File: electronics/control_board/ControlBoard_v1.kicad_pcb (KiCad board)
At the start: 2 copper layers, 64 x 85 mm, 28 parts, among them J1 Motor1, J2 Motor2, J3 Motor3, J4 Encoder, J5 I2C, J7 Power, U1 ROB-14450, U2 ROB-14450, U3 ROB-14450, U4 DCDC_Converter

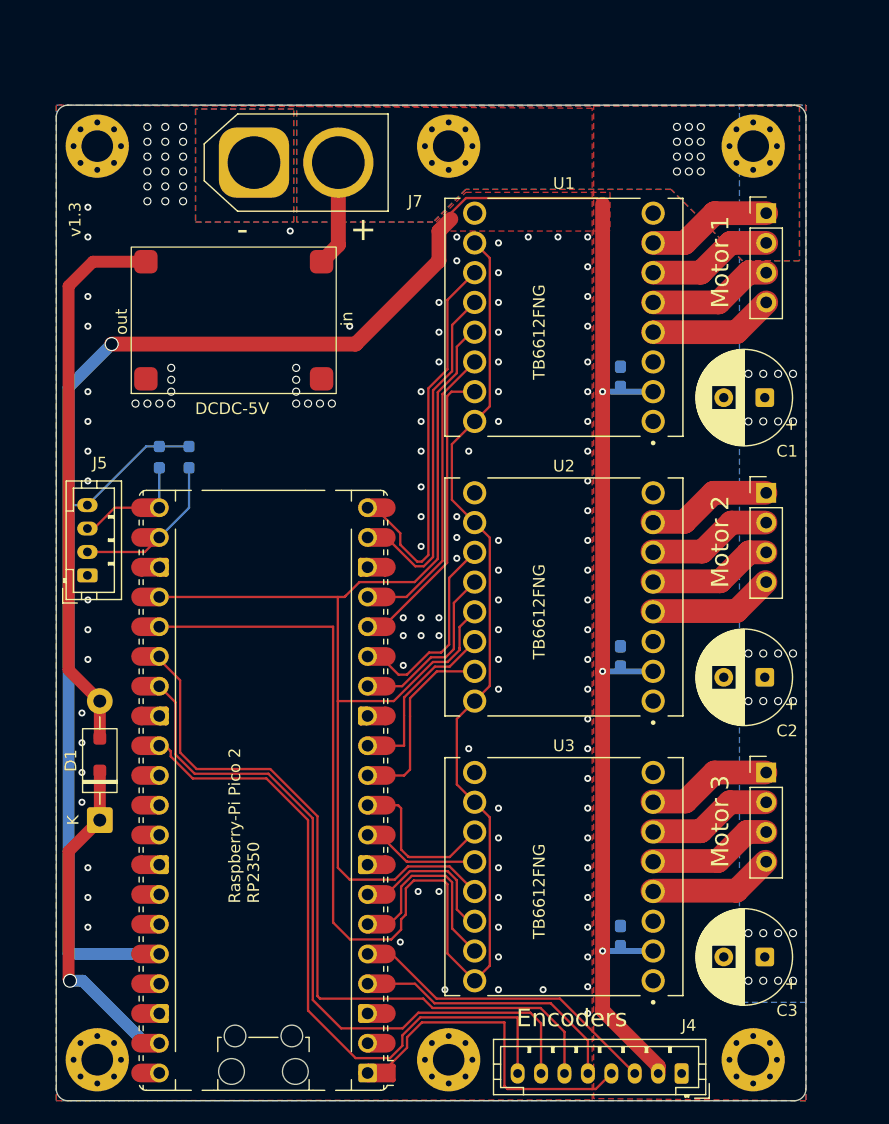
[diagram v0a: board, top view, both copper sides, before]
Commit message: Worked on PCB (moved to 4 layers)
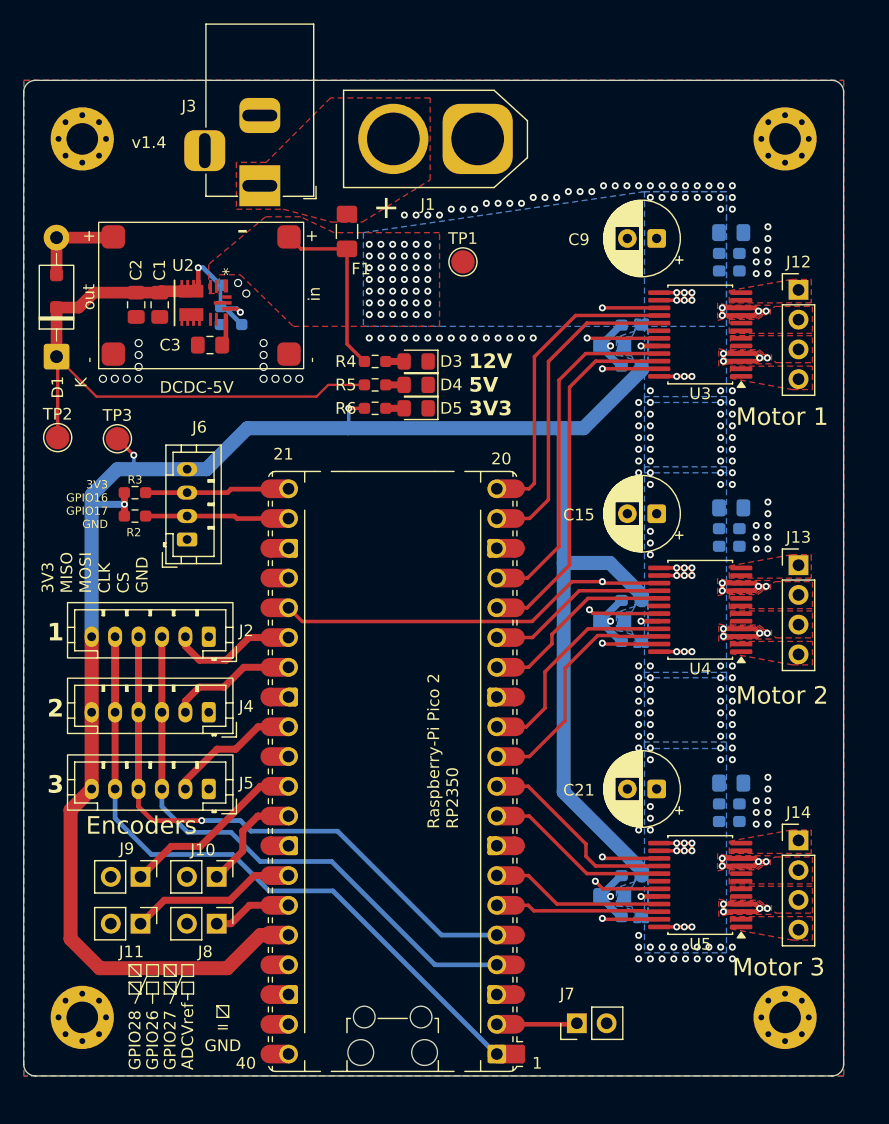
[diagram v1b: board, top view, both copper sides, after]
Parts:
- removed the H5 at (188.3, 120.6)
- removed H6: MountingHole_Pad, MountingHole:MountingHole_2.7mm_M2.5_Pad_Via
- removed the J1 at (215.4, 48.3)
- removed the U1 at (198.1, 57.2)
- added C10: 10u, Capacitor_SMD:C_0805_2012Metric_Pad1.18x1.45mm_HandSolder, B.Cu at (202.2, 83.2)
- added C11: 0.1u, Capacitor_SMD:C_0603_1608Metric_Pad1.08x0.95mm_HandSolder, B.Cu at (203.9, 84.9)
- added C12: 0.1u, Capacitor_SMD:C_0603_1608Metric_Pad1.08x0.95mm_HandSolder, B.Cu at (212.2, 75.3)
- added C13: 0.1u, Capacitor_SMD:C_0603_1608Metric_Pad1.08x0.95mm_HandSolder, B.Cu at (212.2, 76.8)
- added C14: 10u, Capacitor_SMD:C_0805_2012Metric_Pad1.18x1.45mm_HandSolder, B.Cu at (212.4, 73.5)
- added C15: 50u, Capacitor_THT:CP_Radial_D6.3mm_P2.50mm, F.Cu at (206.0, 74.0)
- added C16: 10u, Capacitor_SMD:C_0805_2012Metric_Pad1.18x1.45mm_HandSolder, B.Cu at (202.2, 106.7)
- added C17: 0.1u, Capacitor_SMD:C_0603_1608Metric_Pad1.08x0.95mm_HandSolder, B.Cu at (203.9, 108.4)
- added C18: 0.1u, Capacitor_SMD:C_0603_1608Metric_Pad1.08x0.95mm_HandSolder, B.Cu at (212.2, 98.8)
- added C19: 0.1u, Capacitor_SMD:C_0603_1608Metric_Pad1.08x0.95mm_HandSolder, B.Cu at (212.2, 100.3)
- added C20: 10u, Capacitor_SMD:C_0805_2012Metric_Pad1.18x1.45mm_HandSolder, B.Cu at (212.4, 97.0)
- added C21: 50u, Capacitor_THT:CP_Radial_D6.3mm_P2.50mm, F.Cu at (206.0, 97.5)
- added C22: 0.1u, Capacitor_SMD:C_0603_1608Metric_Pad1.08x0.95mm_HandSolder, B.Cu at (203.9, 57.9)
- added C23: 0.1u, Capacitor_SMD:C_0603_1608Metric_Pad1.08x0.95mm_HandSolder, B.Cu at (203.9, 81.4)
- added C24: 0.1u, Capacitor_SMD:C_0603_1608Metric_Pad1.08x0.95mm_HandSolder, B.Cu at (203.9, 104.9)
- added C7: 0.1u, Capacitor_SMD:C_0603_1608Metric_Pad1.08x0.95mm_HandSolder, B.Cu at (212.2, 53.3)
- added C8: 10u, Capacitor_SMD:C_0805_2012Metric_Pad1.18x1.45mm_HandSolder, B.Cu at (212.4, 50.0)
- added C9: 50u, Capacitor_THT:CP_Radial_D6.3mm_P2.50mm, F.Cu at (206.0, 50.5)
- added D3: 12V_OK, LED_SMD:LED_0805_2012Metric_Pad1.15x1.40mm_HandSolder, F.Cu at (185.5, 61.0)
- added D4: 5V_OK, LED_SMD:LED_0805_2012Metric_Pad1.15x1.40mm_HandSolder, F.Cu at (185.5, 63.0)
- added D5: 3V3_OK, LED_SMD:LED_0805_2012Metric_Pad1.15x1.40mm_HandSolder, F.Cu at (185.5, 65.0)
- added F1: Fuse, Fuse:Fuse_1206_3216Metric_Pad1.42x1.75mm_HandSolder, F.Cu at (179.6, 49.9)
- added J10: Conn_01x02_Pin, Connector_PinHeader_2.54mm:PinHeader_1x02_P2.54mm_Vertical, F.Cu at (168.5, 105.0)
- added J11: Conn_01x02_Pin, Connector_PinHeader_2.54mm:PinHeader_1x02_P2.54mm_Vertical, F.Cu at (162.0, 109.0)
- added J12: Motor1, Connector_PinHeader_2.54mm:PinHeader_1x04_P2.54mm_Vertical, F.Cu at (218.1, 54.9)
- added J13: Motor1, Connector_PinHeader_2.54mm:PinHeader_1x04_P2.54mm_Vertical, F.Cu at (218.1, 78.4)
- added J14: Motor1, Connector_PinHeader_2.54mm:PinHeader_1x04_P2.54mm_Vertical, F.Cu at (218.1, 101.9)
- added J5: Conn_01x06_Pin, Connector_JST:JST_PH_B6B-PH-K_1x06_P2.00mm_Vertical, F.Cu at (167.8, 97.5)
- added J7: Conn_01x02_Pin, Connector_PinHeader_2.54mm:PinHeader_1x02_P2.54mm_Vertical, F.Cu at (199.2, 117.5)
- added J8: Conn_01x02_Pin, Connector_PinHeader_2.54mm:PinHeader_1x02_P2.54mm_Vertical, F.Cu at (168.5, 109.0)
- added J9: Conn_01x02_Pin, Connector_PinHeader_2.54mm:PinHeader_1x02_P2.54mm_Vertical, F.Cu at (162.0, 105.0)
- added R1: TBD, Resistor_SMD:R_0603_1608Metric_Pad0.98x0.95mm_HandSolder, B.Cu at (169.7, 57.8)
- added R4: 1k, Resistor_SMD:R_0603_1608Metric_Pad0.98x0.95mm_HandSolder, F.Cu at (182.0, 61.0)
- added R5: 1k, Resistor_SMD:R_0603_1608Metric_Pad0.98x0.95mm_HandSolder, F.Cu at (182.0, 63.0)
- added R6: 1k, Resistor_SMD:R_0603_1608Metric_Pad0.98x0.95mm_HandSolder, F.Cu at (182.0, 65.0)
- added RJ1: TBD, Additions:0603_shorted_resistor, B.Cu at (168.8, 55.4)
- added TP1: 12V, TestPoint:TestPoint_Pad_D2.0mm, F.Cu at (189.5, 52.5)
- added TP2: 5V, TestPoint:TestPoint_Pad_D2.0mm, F.Cu at (154.9, 67.5)
- added TP3: 3V3, TestPoint:TestPoint_Pad_D2.0mm, F.Cu at (160.0, 67.6)
- added U4: TB6612FNG, Package_SO:SSOP-24_5.3x8.2mm_P0.65mm, F.Cu at (209.8, 82.2)
- added U5: TB6612FNG, Package_SO:SSOP-24_5.3x8.2mm_P0.65mm, F.Cu at (209.8, 105.7)
- C1, C2: value C_Polarized -> 22u; footprint Capacitor_THT:CP_Radial_D8.0mm_P3.50mm -> Capacitor_SMD:C_0805_2012Metric_Pad1.18x1.45mm_HandSolder
- C3: value C_Polarized -> 1u; footprint Capacitor_THT:CP_Radial_D8.0mm_P3.50mm -> Capacitor_SMD:C_0805_2012Metric_Pad1.18x1.45mm_HandSolder
- C4: value C -> 10u; footprint Capacitor_SMD:C_0603_1608Metric_Pad1.08x0.95mm_HandSolder -> Capacitor_SMD:C_0805_2012Metric_Pad1.18x1.45mm_HandSolder
- C5, C6: value C -> 0.1u
- J2: value Motor2 -> Conn_01x06_Pin; footprint Connector_PinHeader_2.54mm:PinHeader_1x04_P2.54mm_Vertical -> Connector_JST:JST_PH_B6B-PH-K_1x06_P2.00mm_Vertical
- J3: value Motor3 -> Barrel_Jack_Switch; footprint Connector_PinHeader_2.54mm:PinHeader_1x04_P2.54mm_Vertical -> Connector_BarrelJack:BarrelJack_Horizontal
- J4: value Encoder -> Conn_01x06_Pin; footprint Connector_JST:JST_PH_B8B-PH-K_1x08_P2.00mm_Vertical -> Connector_JST:JST_PH_B6B-PH-K_1x06_P2.00mm_Vertical
- R2: moved to F.Cu
- R3: renamed from R1; moved to F.Cu
- U2: value ROB-14450 -> TPSM33610S5QRDNRQ1; footprint ROB-14450:MODULE_ROB-14450 -> Additions:TPSM33610S5QRDNRQ1
- U3: value ROB-14450 -> TB6612FNG; footprint ROB-14450:MODULE_ROB-14450 -> Package_SO:SSOP-24_5.3x8.2mm_P0.65mm
- moved C3 70.5 mm to (167.9, 59.6)
- moved J3 66.2 mm to (172.2, 46.0), turned to -90 degrees
- moved C2 62.4 mm to (161.6, 56.2), turned to -90 degrees
- moved C6 59.0 mm to (212.2, 51.8), turned to 0 degrees
- moved C1 52.3 mm to (163.6, 56.2), turned to -90 degrees
- moved J4 50.8 mm to (167.8, 91.0)
- moved J2 49.2 mm to (167.8, 84.5), turned to 180 degrees
- moved U3 47.7 mm to (209.8, 58.7)
- moved U2 39.8 mm to (167.3, 56.0), turned to -90 degrees
- moved D1 39.7 mm to (154.8, 60.6)
- moved D2 39.7 mm to (154.8, 55.0)
- moved C5 24.8 mm to (203.9, 61.4), turned to 180 degrees
- moved J1 19.2 mm to (190.8, 42.0), turned to 180 degrees
- moved REF** 17.3 mm to (166.2, 116.2)
- moved A1 11.2 mm to (183.5, 96.0)
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- renumbered H4 to H2, H2 to H3, H3 to H5, J7 to J1, J5 to J6, U4 to U1
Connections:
- A1 pad 2: unconnected-(A1-GPIO1-Pad2)_1 -> /GPIO1
- A1 pad 31: unconnected-(A1-GPIO26_ADC0-Pad31)_1 -> /GPIO26_ADC0
- A1 pad 32: unconnected-(A1-GPIO27_ADC1-Pad32)_1 -> /GPIO27_ADC1
- A1 pad 34: unconnected-(A1-GPIO28_ADC2-Pad34)_1 -> /GPIO28_ADC2
- A1 pad 35: unconnected-(A1-ADC_VREF-Pad35)_1 -> /ADC_VREF
- C1 pad 1: +12V -> +5V
- C2 pad 1: +12V -> +5V
- C3 pad 1: +12V -> Net-(U2-VCC)
- C6 pad 1: +3.3V -> +12V
- H1 pad 1: unconnected-(H1-Pad1)_6 -> GND
- H2 pad 1: unconnected-(H4-Pad1)_5 -> GND
- H3 pad 1: unconnected-(H2-Pad1)_2 -> GND
- H5 pad 1: unconnected-(H3-Pad1)_6 -> GND
- J1 pad 2: +12V -> Net-(J1-Pin_2)
- J2 pad 1: Net-(J2-Pin_1) -> GND
- J2 pad 2: Net-(J2-Pin_2) -> /Encoder1_CS
- J2 pad 3: Net-(J2-Pin_3) -> /Encoder_SCK
- J2 pad 4: Net-(J2-Pin_4) -> /Encoder_MOSI
- J3 pad 1: Net-(J3-Pin_1) -> Net-(J1-Pin_2)
- J3 pad 2: Net-(J3-Pin_2) -> GND
- J3 pad 3: Net-(J3-Pin_3) -> GND
- J4 pad 2: +3.3V -> /Encoder2_CS
- J4 pad 3: /Encoder_MOSI -> /Encoder_SCK
- J4 pad 4: /Encoder_MISO -> /Encoder_MOSI
- J4 pad 5: /Encoder_SCK -> /Encoder_MISO
- J4 pad 6: /Encoder1_CS -> +3.3V
- U2 pad 1: +12V -> unconnected-(U2-PGOOD-Pad1)
- U2 pad 10: /MotorPWM -> GND
- U2 pad 11: /Motor2_B2 -> GND
- U2 pad 2: +3.3V -> +12V
- U2 pad 3: GND -> +12V
- U2 pad 4: Net-(J2-Pin_4) -> +5V
- U2 pad 5: Net-(J2-Pin_3) -> unconnected-(U2-SW-Pad5)
- U2 pad 6: Net-(J2-Pin_2) -> unconnected-(U2-SW-Pad6)
- U2 pad 7: Net-(J2-Pin_1) -> unconnected-(U2-BOOT-Pad7)
- U2 pad 8: GND -> Net-(U2-VCC)
- U2 pad 9: GND -> Net-(U2-FB)
- U3 pad 1: +12V -> Net-(J12-Pin_4)
- U3 pad 10: /MotorPWM -> GND
- U3 pad 11: /Motor3_B2 -> Net-(J12-Pin_1)
- U3 pad 12: /Motor3_B1 -> Net-(J12-Pin_1)
- U3 pad 13: /MotorEN -> +12V
- U3 pad 14: /Motor3_A1 -> +12V
- U3 pad 15: /Motor3_A2 -> /MotorPWM
- U3 pad 16: /MotorPWM -> /Motor1_B2
- U3 pad 2: +3.3V -> Net-(J12-Pin_4)
- U3 pad 4: Net-(J3-Pin_4) -> GND
- U3 pad 5: Net-(J3-Pin_3) -> Net-(J12-Pin_3)
- U3 pad 6: Net-(J3-Pin_2) -> Net-(J12-Pin_3)
- U3 pad 7: Net-(J3-Pin_1) -> Net-(J12-Pin_2)
- U3 pad 8: GND -> Net-(J12-Pin_2)
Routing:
- net +5V: track 28.4 -> 127.8 mm
- net GND: track 0.00 -> 64.6 mm, vias 129 -> 163
- net /Encoder1_CS: track 64.2 -> 10.1 mm
- net /Encoder2_CS: track 61.6 -> 10.2 mm
- net /Encoder3_CS: track 58.2 -> 10.6 mm
- net Net-(D1-A): track 47.2 -> 7.96 mm
- net +12V: track 9.05 -> 47.0 mm, vias 36 -> 126
- net +3.3V: track 211.7 -> 176.5 mm, vias 4 -> 6
- net /Encoder_MISO: track 29.4 -> 62.8 mm
- net /Encoder_SCK: track 23.8 -> 48.7 mm
- net /MotorPWM: track 132.8 -> 111.4 mm, vias 0 -> 6
- net /Encoder_MOSI: track 28.8 -> 49.6 mm, vias 0 -> 1
- net /GPIO26_ADC0: track 0.00 -> 15.0 mm
- net /GPIO28_ADC2: track 0.00 -> 13.5 mm
- net Net-(J1-Pin_4): track 10.7 -> 0.00 mm
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- added copper zone on In2.Cu, net +12V
- added copper zone on B.Cu, net +3.3V
- added copper zone on In1.Cu, net GND
- added copper zone on F.Cu, net Net-(J1-Pin_2)
- added copper zone on F.Cu, net Net-(J12-Pin_1)
- added copper zone on F.Cu, net Net-(J12-Pin_2)
- added copper zone on F.Cu, net Net-(J12-Pin_3)
- added copper zone on F.Cu, net Net-(J12-Pin_4)
- added copper zone on F.Cu, net Net-(J13-Pin_1)
- added copper zone on F.Cu, net Net-(J13-Pin_2)
- added copper zone on F.Cu, net Net-(J13-Pin_3)
- added copper zone on F.Cu, net Net-(J13-Pin_4)
- added copper zone on F.Cu, net Net-(J14-Pin_1)
- added copper zone on F.Cu, net Net-(J14-Pin_2)
- added copper zone on F.Cu, net Net-(J14-Pin_3)
- added copper zone on F.Cu, net Net-(J14-Pin_4)
- removed copper zone on F.Cu, net +3.3V
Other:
- board size 64 x 85 mm -> 70 x 85 mm
- copper layers 2 -> 4
- board text added: "1"
- board text added: "12V 5V 3V3"
- board text added: "2"
- board text added: "20"
- board text added: "21"
- board text added: "3"
- board text added: "3V3 GPIO16 GPIO17 GND"
- board text added: "3V3 MISO MOSI CLK CS GND"
- board text added: "40"
- board text added: "= GND"
- board text added: "ADCVref"
- board text added: "GPIO26"
- board text added: "GPIO27"
- board text added: "GPIO28"
- board text added: "v1.4"
- board text removed: "(00) MISO"
- board text removed: "(03) MOSI"
- board text removed: "(20) CS_1"
- board text removed: "(21) CS_2"
- board text removed: "(22) CS_3"
- board text removed: "(O2) SCK"
- board text removed: "3.3V"
- board text removed: "GND"
- board text removed: "GPIO16"
- board text removed: "GPIO17"
- board text removed: "M1_A1 (13) M1_A2 (12) M1_B1 (14) M1_B2 (15)"
- board text removed: "M2_A1 (09) M2_A2 (08) M2_B1 (10) M2_B2 (11)"
- board text removed: "M3_A1 (05) M3_A2 (04) M3_B1 (06) M3_B2 (07)"
- board text removed: "MotorEN (18)"
- board text removed: "MotorPWM (19)"
- board text removed: "Precision Stepper Controller 3X"
- board text removed: "TB6612FNG"
- board text removed: "v1.3"

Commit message: Worked on schematic and layout Added logo
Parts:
- added C1: 0.1u, Capacitor_SMD:C_0603_1608Metric_Pad1.08x0.95mm_HandSolder, F.Cu at (167.6, 51.8)
- added C2: 22u, Capacitor_SMD:C_0805_2012Metric_Pad1.18x1.45mm_HandSolder, F.Cu at (167.4, 50.0)
- added R10: 4K7, Resistor_SMD:R_0603_1608Metric_Pad0.98x0.95mm_HandSolder, B.Cu at (169.7, 79.5)
- added R4: 4K7, Resistor_SMD:R_0603_1608Metric_Pad0.98x0.95mm_HandSolder, B.Cu at (164.9, 94.1)
- added R5: 4K7, Resistor_SMD:R_0603_1608Metric_Pad0.98x0.95mm_HandSolder, B.Cu at (164.9, 87.9)
- added R6: 4K7, Resistor_SMD:R_0603_1608Metric_Pad0.98x0.95mm_HandSolder, B.Cu at (164.9, 81.8)
- added REF**: Logo, Additions:Logo, F.Cu at (183.4, 88.0)
- C12: renamed from C9; value 50u -> 100u
- C19: renamed from C15; value 50u -> 100u
- C26: renamed from C21; value 50u -> 100u
- F1: value Fuse -> 7A
- J12, J13, J14: value Motor1 -> ~
- R7: renamed from R4; value 1k -> 4k7
- moved R2 2.00 mm to (161.5, 72.2)
- moved R3 2.00 mm to (161.5, 74.2)
- moved D5 0.10 mm to (185.5, 64.9)
- moved R9 0.10 mm to (182.0, 64.9)
- renumbered C7 to C10, C8 to C11, C10 to C13, C11 to C14, C23 to C15, C12 to C16, C13 to C17, C14 to C18, C16 to C20, C17 to C21, C24 to C22, C18 to C23, C19 to C24, C20 to C25, C1 to C3, C2 to C4, C3 to C5, C4 to C6, C5 to C7, C22 to C8, C6 to C9, H5 to H4, R5 to R8, R6 to R9
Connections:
- A1 pad 21: /I2C_SCL -> /I2C_SDA
- A1 pad 22: /I2C_SDA -> /I2C_SCL
- R2 pad 2: /I2C_SDA -> /I2C_SCL
- R3 pad 2: /I2C_SCL -> /I2C_SDA
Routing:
- net +3.3V: track 176.5 -> 199.1 mm
- net +12V: track 47.0 -> 66.6 mm
- net /I2C_SCL: track 11.5 -> 19.0 mm
- net /MotorEN: track 90.7 -> 94.7 mm
- net /Encoder3_CS: track 10.6 -> 14.0 mm
- net /Encoder2_CS: track 10.2 -> 13.2 mm
- net /Encoder1_CS: track 10.1 -> 12.7 mm
- net /I2C_SDA: track 11.5 -> 12.4 mm

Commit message: Worked on PCB and Schematic, created production files
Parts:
- added D3: SMAJ12CA, Diode_SMD:D_SMA_Handsoldering, B.Cu at (208.8, 45.8)
- moved TP1 1.50 mm to (189.4, 54.0)
- moved C12 1.50 mm to (206.0, 49.0)
- moved REF** 0.39 mm to (183.5, 88.4)
- renumbered D3 to D4, D4 to D5, D5 to D6
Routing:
- net +12V: track 66.6 -> 95.3 mm, vias 126 -> 80
- net +3.3V: track 199.1 -> 227.3 mm, vias 6 -> 27
- net /MotorPWM: track 111.4 -> 121.5 mm
- net +5V: track 127.8 -> 135.0 mm, vias 1 -> 7
- net GND: track 64.6 -> 70.5 mm, vias 163 -> 224
- net /MotorEN: track 94.7 -> 97.8 mm
- net /I2C_SCL: track 19.0 -> 19.9 mm
- added copper zone on F.Cu, net +3.3V
- added copper zone on In2.Cu, net +3.3V
- added copper zone on F.Cu, net +5V
- added copper zone on In2.Cu, net +5V
- added copper zone on In2.Cu, net GND
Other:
- board text added: "12V"
- board text added: "3V3"
- board text added: "5V"
- board text added: "GPIO1 GND"
- board text removed: "= GND"

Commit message: Fixed wrong ordering numbers Regenerated IBOM with corrected settings to exclude TP's
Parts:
- R10, R2, R3, R4, R5, R6: value 4K7 -> 4k7
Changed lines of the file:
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@@
 			)
 		)
+		(property "Distributor" "Digikey"
+			(at 0 0 0)
+			(unlocked yes)
+			(layer "F.Fab")
+			(hide yes)
+			(effects
+				(font
+					(size 1 1)
+					(thickness 0.15)
+				)
+			)
+		)
+		(property "Distributor Number" "541-4.70KHCT-ND"
+			(at 0 0 0)
+			(unlocked yes)
+			(layer "F.Fab")
+			(hide yes)
+			(effects
+				(font
+					(size 1 1)
+					(thickness 0.15)
+				)
+			)
+		)
 		(property ki_fp_filters "R_*")
 		(sheetname "/")
@@
 			)
 		)
+		(property "Distributor" "-"
+			(at 0 0 0)
+			(unlocked yes)
+			(layer "F.Fab")
+			(hide yes)
+			(effects
+				(font
+					(size 1 1)
+					(thickness 0.15)
+				)
+			)
+		)
+		(property "Distributor Number" "-"
+			(at 0 0 0)
+			(unlocked yes)
+			(layer "F.Fab")
+			(hide yes)
+			(effects
+				(font
+					(size 1 1)
+					(thickness 0.15)
+				)
+			)
+		)
 		(property ki_fp_filters "Pin* Test*")
 		(sheetname "/")
@@
 			)
 		)
+		(attr exclude_from_bom)
 		(duplicate_pad_numbers_are_jumpers no)
 		(fp_circle
@@
 			)
 		)
+		(property "Distributor" "?"
+			(at 0 0 180)
+			(unlocked yes)
+			(layer "F.Fab")
+			(hide yes)
+			(effects
+				(font
+					(size 1 1)
+					(thickness 0.15)
+				)
+			)
+		)
+		(property "Distributor Number" "-"
+			(at 0 0 180)
+			(unlocked yes)
+			(layer "F.Fab")
+			(hide yes)
+			(effects
+				(font
+					(size 1 1)
+					(thickness 0.15)
+				)
+			)
+		)
 		(property ki_fp_filters "LED* LED_SMD:* LED_THT:*")
 		(sheetname "/")
@@
 			)
 		)
-		(property "Value" "4K7"
+		(property "Value" "4k7"
 			(at 0 1.43 0)
 			(layer "F.Fab")
@@
 			)
 		)
-		(property "Distributor Number" "455-B6B-XH-A-ND"
+		(property "Distributor Number" "455-1708-ND"
 			(at 0 0 180)
 			(unlocked yes)
@@
 			)
 		)
+		(property "Distributor" "-"
+			(at 0 0 0)
+			(unlocked yes)
+			(layer "F.Fab")
+			(hide yes)
+			(effects
+				(font
+					(size 1 1)
+					(thickness 0.15)
+				)
+			)
+		)
+		(property "Distributor Number" "-"
+			(at 0 0 0)
+			(unlocked yes)
+			(layer "F.Fab")
+			(hide yes)
+			(effects
+				(font
+					(size 1 1)
+					(thickness 0.15)
+				)
+			)
+		)
 		(property ki_fp_filters "Pin* Test*")
 		(sheetname "/")
@@
 			)
 		)
+		(attr exclude_from_bom)
 		(duplicate_pad_numbers_are_jumpers no)
 		(fp_circle
@@
 			)
 		)
+		(property "Distributor" "-"
+			(at 0 0 0)
+			(unlocked yes)
+			(layer "F.Fab")
+			(hide yes)
+			(effects
+				(font
+					(size 1 1)
+					(thickness 0.15)
+				)
+			)
+		)
+		(property "Distributor Number" "-"
+			(at 0 0 0)
+			(unlocked yes)
+			(layer "F.Fab")
+			(hide yes)
+			(effects
+				(font
+					(size 1 1)
+					(thickness 0.15)
+				)
+			)
+		)
 		(property ki_fp_filters "Pin* Test*")
 		(sheetname "/")
@@
 			)
 		)
+		(attr exclude_from_bom)
 		(duplicate_pad_numbers_are_jumpers no)
 		(fp_circle
@@
 			)
 		)
+		(property "Distributor" "?"
+			(at 0 0 180)
+			(unlocked yes)
+			(layer "F.Fab")
+			(hide yes)
+			(effects
+				(font
+					(size 1 1)
+					(thickness 0.15)
+				)
+			)
+		)
+		(property "Distributor Number" "-"
+			(at 0 0 180)
+			(unlocked yes)
+			(layer "F.Fab")
+			(hide yes)
+			(effects
+				(font
+					(size 1 1)
+					(thickness 0.15)
+				)
+			)
+		)
 		(property ki_fp_filters "LED* LED_SMD:* LED_THT:*")
 		(sheetname "/")
@@
 			)
 		)
+		(property "Distributor" "?"
+			(at 0 0 180)
+			(unlocked yes)
+			(layer "F.Fab")
+			(hide yes)
+			(effects
+				(font
+					(size 1 1)
+					(thickness 0.15)
+				)
+			)
+		)
+		(property "Distributor Number" "-"
+			(at 0 0 180)
+			(unlocked yes)
+			(layer "F.Fab")
+			(hide yes)
+			(effects
+				(font
+					(size 1 1)
+					(thickness 0.15)
+				)
+			)
+		)
 		(property ki_fp_filters "LED* LED_SMD:* LED_THT:*")
 		(sheetname "/")
@@
 			)
 		)
+		(property "Distributor" "Digikey"
+			(at 0 0 0)
+			(unlocked yes)
+			(layer "F.Fab")
+			(hide yes)
+			(effects
+				(font
+					(size 1 1)
+					(thickness 0.15)
+				)
+			)
+		)
+		(property "Distributor Number" "541-1.00KHCT-ND"
+			(at 0 0 0)
+			(unlocked yes)
+			(layer "F.Fab")
+			(hide yes)
+			(effects
+				(font
+					(size 1 1)
+					(thickness 0.15)
+				)
+			)
+		)
 		(property ki_fp_filters "R_*")
 		(sheetname "/")
@@
 			)
 		)
-		(property "Distributor Number" "455-B6B-XH-A-ND"
+		(property "Distributor Number" "455-1708-ND"
 			(at 0 0 180)
 			(unlocked yes)
@@
 			)
 		)
-		(property "Distributor Number" "455-B4B-XH-A-ND"
+		(property "Distributor Number" "455-1706-ND"
 			(at 0 0 90)
 			(unlocked yes)
@@
 			)
 		)
-		(property "Value" "4K7"
+		(property "Value" "4k7"
 			(at 0 1.43 0)
 			(layer "F.Fab")
@@
 			)
 		)
-		(property "Distributor Number" "455-B6B-XH-A-ND"
+		(property "Distributor Number" "455-1708-ND"
 			(at 0 0 180)
 			(unlocked yes)
@@
 			)
 		)
+		(property "Distributor" "Digikey"
+			(at 0 0 0)
+			(unlocked yes)
+			(layer "F.Fab")
+			(hide yes)
+			(effects
+				(font
+					(size 1 1)
+					(thickness 0.15)
+				)
+			)
+		)
+		(property "Distributor Number" "541-1.00KHCT-ND"
+			(at 0 0 0)
+			(unlocked yes)
+			(layer "F.Fab")
+			(hide yes)
+			(effects
+				(font
+					(size 1 1)
+					(thickness 0.15)
+				)
+			)
+		)
 		(property ki_fp_filters "R_*")
 		(sheetname "/")
@@
 			)
 		)
-		(property "Value" "4K7"
+		(property "Value" "4k7"
 			(at 0 -1.43 0)
 			(layer "B.Fab")
@@
 			)
 		)
-		(property "Value" "4K7"
+		(property "Value" "4k7"
 			(at 0 -1.43 0)
 			(layer "B.Fab")
@@
 			)
 		)
-		(property "Value" "4K7"
+		(property "Value" "4k7"
 			(at 0 -1.43 0)
 			(layer "B.Fab")
@@
 			)
 		)
-		(property "Value" "4K7"
+		(property "Value" "4k7"
 			(at 0 -1.43 0)
 			(layer "B.Fab")
